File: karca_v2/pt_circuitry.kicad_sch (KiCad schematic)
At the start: 11 parts, among them U7 TLV9304xD, U8 TLV9304xD

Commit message: discrete traces
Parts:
- renumbered C19 to C34, C20 to C35
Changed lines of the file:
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@@
         )
         (path "/29cf4797-56f2-4f57-ae95-7df639362e3c/c566ee8f-cb19-4e44-a9af-dd67a0aa158e/60027281-032f-4987-83fe-1472a08d0df6"
-          (reference "R90") (unit 1)
+          (reference "R94") (unit 1)
         )
       )
@@
         )
         (path "/29cf4797-56f2-4f57-ae95-7df639362e3c/c566ee8f-cb19-4e44-a9af-dd67a0aa158e/60027281-032f-4987-83fe-1472a08d0df6"
-          (reference "R92") (unit 1)
+          (reference "R96") (unit 1)
         )
       )
@@
   (symbol (lib_id "power:GND") (at 168.656 89.916 0) (unit 1)
     (in_bom yes) (on_board yes) (dnp no) (fields_autoplaced)
-    (property "Reference" "#PWR091" (at 168.656 96.266 0)
+    (property "Reference" "#PWR0106" (at 168.656 96.266 0)
       (effects (font (size 1.27 1.27)) hide)
     )
@@
       (project "karca_v2"
         (path "/29cf4797-56f2-4f57-ae95-7df639362e3c/c566ee8f-cb19-4e44-a9af-dd67a0aa158e/044bcd6a-880d-4ffc-be8b-a03d76768183"
-          (reference "#PWR091") (unit 1)
-        )
-        (path "/29cf4797-56f2-4f57-ae95-7df639362e3c/c566ee8f-cb19-4e44-a9af-dd67a0aa158e/691cd68e-b9d2-4323-a044-22fc45a3ad38"
-          (reference "#PWR094") (unit 1)
-        )
-        (path "/29cf4797-56f2-4f57-ae95-7df639362e3c/c566ee8f-cb19-4e44-a9af-dd67a0aa158e/c6078a97-3f1f-4f19-8ed7-752ec56dbc3c"
-          (reference "#PWR097") (unit 1)
-        )
-        (path "/29cf4797-56f2-4f57-ae95-7df639362e3c/c566ee8f-cb19-4e44-a9af-dd67a0aa158e/60027281-032f-4987-83fe-1472a08d0df6"
-          (reference "#PWR0145") (unit 1)
+          (reference "#PWR0106") (unit 1)
+        )
+        (path "/29cf4797-56f2-4f57-ae95-7df639362e3c/c566ee8f-cb19-4e44-a9af-dd67a0aa158e/691cd68e-b9d2-4323-a044-22fc45a3ad38"
+          (reference "#PWR0109") (unit 1)
+        )
+        (path "/29cf4797-56f2-4f57-ae95-7df639362e3c/c566ee8f-cb19-4e44-a9af-dd67a0aa158e/c6078a97-3f1f-4f19-8ed7-752ec56dbc3c"
+          (reference "#PWR0112") (unit 1)
+        )
+        (path "/29cf4797-56f2-4f57-ae95-7df639362e3c/c566ee8f-cb19-4e44-a9af-dd67a0aa158e/60027281-032f-4987-83fe-1472a08d0df6"
+          (reference "#PWR0168") (unit 1)
         )
       )
@@
   (symbol (lib_id "Device:C") (at 191.516 58.166 270) (unit 1)
     (in_bom yes) (on_board yes) (dnp no) (fields_autoplaced)
-    (property "Reference" "C19" (at 191.516 50.546 90)
+    (property "Reference" "C34" (at 191.516 50.546 90)
       (effects (font (size 1.27 1.27)))
     )
@@
       (project "karca_v2"
         (path "/29cf4797-56f2-4f57-ae95-7df639362e3c/c566ee8f-cb19-4e44-a9af-dd67a0aa158e/044bcd6a-880d-4ffc-be8b-a03d76768183"
-          (reference "C19") (unit 1)
-        )
-        (path "/29cf4797-56f2-4f57-ae95-7df639362e3c/c566ee8f-cb19-4e44-a9af-dd67a0aa158e/691cd68e-b9d2-4323-a044-22fc45a3ad38"
-          (reference "C21") (unit 1)
-        )
-        (path "/29cf4797-56f2-4f57-ae95-7df639362e3c/c566ee8f-cb19-4e44-a9af-dd67a0aa158e/c6078a97-3f1f-4f19-8ed7-752ec56dbc3c"
-          (reference "C23") (unit 1)
-        )
-        (path "/29cf4797-56f2-4f57-ae95-7df639362e3c/c566ee8f-cb19-4e44-a9af-dd67a0aa158e/60027281-032f-4987-83fe-1472a08d0df6"
-          (reference "C49") (unit 1)
+          (reference "C34") (unit 1)
+        )
+        (path "/29cf4797-56f2-4f57-ae95-7df639362e3c/c566ee8f-cb19-4e44-a9af-dd67a0aa158e/691cd68e-b9d2-4323-a044-22fc45a3ad38"
+          (reference "C36") (unit 1)
+        )
+        (path "/29cf4797-56f2-4f57-ae95-7df639362e3c/c566ee8f-cb19-4e44-a9af-dd67a0aa158e/c6078a97-3f1f-4f19-8ed7-752ec56dbc3c"
+          (reference "C38") (unit 1)
+        )
+        (path "/29cf4797-56f2-4f57-ae95-7df639362e3c/c566ee8f-cb19-4e44-a9af-dd67a0aa158e/60027281-032f-4987-83fe-1472a08d0df6"
+          (reference "C64") (unit 1)
         )
       )
@@
   (symbol (lib_id "power:GND") (at 86.106 83.566 0) (unit 1)
     (in_bom yes) (on_board yes) (dnp no) (fields_autoplaced)
-    (property "Reference" "#PWR090" (at 86.106 89.916 0)
+    (property "Reference" "#PWR0105" (at 86.106 89.916 0)
       (effects (font (size 1.27 1.27)) hide)
     )
@@
       (project "karca_v2"
         (path "/29cf4797-56f2-4f57-ae95-7df639362e3c/c566ee8f-cb19-4e44-a9af-dd67a0aa158e/044bcd6a-880d-4ffc-be8b-a03d76768183"
-          (reference "#PWR090") (unit 1)
-        )
-        (path "/29cf4797-56f2-4f57-ae95-7df639362e3c/c566ee8f-cb19-4e44-a9af-dd67a0aa158e/691cd68e-b9d2-4323-a044-22fc45a3ad38"
-          (reference "#PWR093") (unit 1)
-        )
-        (path "/29cf4797-56f2-4f57-ae95-7df639362e3c/c566ee8f-cb19-4e44-a9af-dd67a0aa158e/c6078a97-3f1f-4f19-8ed7-752ec56dbc3c"
-          (reference "#PWR096") (unit 1)
-        )
-        (path "/29cf4797-56f2-4f57-ae95-7df639362e3c/c566ee8f-cb19-4e44-a9af-dd67a0aa158e/60027281-032f-4987-83fe-1472a08d0df6"
-          (reference "#PWR0144") (unit 1)
+          (reference "#PWR0105") (unit 1)
+        )
+        (path "/29cf4797-56f2-4f57-ae95-7df639362e3c/c566ee8f-cb19-4e44-a9af-dd67a0aa158e/691cd68e-b9d2-4323-a044-22fc45a3ad38"
+          (reference "#PWR0108") (unit 1)
+        )
+        (path "/29cf4797-56f2-4f57-ae95-7df639362e3c/c566ee8f-cb19-4e44-a9af-dd67a0aa158e/c6078a97-3f1f-4f19-8ed7-752ec56dbc3c"
+          (reference "#PWR0111") (unit 1)
+        )
+        (path "/29cf4797-56f2-4f57-ae95-7df639362e3c/c566ee8f-cb19-4e44-a9af-dd67a0aa158e/60027281-032f-4987-83fe-1472a08d0df6"
+          (reference "#PWR0167") (unit 1)
         )
       )
@@
   (symbol (lib_id "power:GND") (at 205.486 108.966 0) (unit 1)
     (in_bom yes) (on_board yes) (dnp no) (fields_autoplaced)
-    (property "Reference" "#PWR092" (at 205.486 115.316 0)
+    (property "Reference" "#PWR0107" (at 205.486 115.316 0)
       (effects (font (size 1.27 1.27)) hide)
     )
@@
       (project "karca_v2"
         (path "/29cf4797-56f2-4f57-ae95-7df639362e3c/c566ee8f-cb19-4e44-a9af-dd67a0aa158e/044bcd6a-880d-4ffc-be8b-a03d76768183"
-          (reference "#PWR092") (unit 1)
-        )
-        (path "/29cf4797-56f2-4f57-ae95-7df639362e3c/c566ee8f-cb19-4e44-a9af-dd67a0aa158e/691cd68e-b9d2-4323-a044-22fc45a3ad38"
-          (reference "#PWR095") (unit 1)
-        )
-        (path "/29cf4797-56f2-4f57-ae95-7df639362e3c/c566ee8f-cb19-4e44-a9af-dd67a0aa158e/c6078a97-3f1f-4f19-8ed7-752ec56dbc3c"
-          (reference "#PWR098") (unit 1)
-        )
-        (path "/29cf4797-56f2-4f57-ae95-7df639362e3c/c566ee8f-cb19-4e44-a9af-dd67a0aa158e/60027281-032f-4987-83fe-1472a08d0df6"
-          (reference "#PWR0146") (unit 1)
+          (reference "#PWR0107") (unit 1)
+        )
+        (path "/29cf4797-56f2-4f57-ae95-7df639362e3c/c566ee8f-cb19-4e44-a9af-dd67a0aa158e/691cd68e-b9d2-4323-a044-22fc45a3ad38"
+          (reference "#PWR0110") (unit 1)
+        )
+        (path "/29cf4797-56f2-4f57-ae95-7df639362e3c/c566ee8f-cb19-4e44-a9af-dd67a0aa158e/c6078a97-3f1f-4f19-8ed7-752ec56dbc3c"
+          (reference "#PWR0113") (unit 1)
+        )
+        (path "/29cf4797-56f2-4f57-ae95-7df639362e3c/c566ee8f-cb19-4e44-a9af-dd67a0aa158e/60027281-032f-4987-83fe-1472a08d0df6"
+          (reference "#PWR0169") (unit 1)
         )
       )
@@
         )
         (path "/29cf4797-56f2-4f57-ae95-7df639362e3c/c566ee8f-cb19-4e44-a9af-dd67a0aa158e/60027281-032f-4987-83fe-1472a08d0df6"
-          (reference "R91") (unit 1)
+          (reference "R95") (unit 1)
         )
       )
@@
         )
         (path "/29cf4797-56f2-4f57-ae95-7df639362e3c/c566ee8f-cb19-4e44-a9af-dd67a0aa158e/60027281-032f-4987-83fe-1472a08d0df6"
-          (reference "R89") (unit 1)
+          (reference "R93") (unit 1)
         )
       )
@@
   (symbol (lib_id "Device:C") (at 168.656 79.756 0) (unit 1)
     (in_bom yes) (on_board yes) (dnp no) (fields_autoplaced)
-    (property "Reference" "C20" (at 171.831 78.486 0)
+    (property "Reference" "C35" (at 171.831 78.486 0)
       (effects (font (size 1.27 1.27)) (justify left))
     )
@@
       (project "karca_v2"
         (path "/29cf4797-56f2-4f57-ae95-7df639362e3c/c566ee8f-cb19-4e44-a9af-dd67a0aa158e/044bcd6a-880d-4ffc-be8b-a03d76768183"
-          (reference "C20") (unit 1)
-        )
-        (path "/29cf4797-56f2-4f57-ae95-7df639362e3c/c566ee8f-cb19-4e44-a9af-dd67a0aa158e/691cd68e-b9d2-4323-a044-22fc45a3ad38"
-          (reference "C22") (unit 1)
-        )
-        (path "/29cf4797-56f2-4f57-ae95-7df639362e3c/c566ee8f-cb19-4e44-a9af-dd67a0aa158e/c6078a97-3f1f-4f19-8ed7-752ec56dbc3c"
-          (reference "C24") (unit 1)
-        )
-        (path "/29cf4797-56f2-4f57-ae95-7df639362e3c/c566ee8f-cb19-4e44-a9af-dd67a0aa158e/60027281-032f-4987-83fe-1472a08d0df6"
-          (reference "C50") (unit 1)
+          (reference "C35") (unit 1)
+        )
+        (path "/29cf4797-56f2-4f57-ae95-7df639362e3c/c566ee8f-cb19-4e44-a9af-dd67a0aa158e/691cd68e-b9d2-4323-a044-22fc45a3ad38"
+          (reference "C37") (unit 1)
+        )
+        (path "/29cf4797-56f2-4f57-ae95-7df639362e3c/c566ee8f-cb19-4e44-a9af-dd67a0aa158e/c6078a97-3f1f-4f19-8ed7-752ec56dbc3c"
+          (reference "C39") (unit 1)
+        )
+        (path "/29cf4797-56f2-4f57-ae95-7df639362e3c/c566ee8f-cb19-4e44-a9af-dd67a0aa158e/60027281-032f-4987-83fe-1472a08d0df6"
+          (reference "C65") (unit 1)
         )
       )
@@
         )
         (path "/29cf4797-56f2-4f57-ae95-7df639362e3c/c566ee8f-cb19-4e44-a9af-dd67a0aa158e/60027281-032f-4987-83fe-1472a08d0df6"
-          (reference "R93") (unit 1)
-        )
-      )
+          (reference "R97") (unit 1)
+        )
+      )

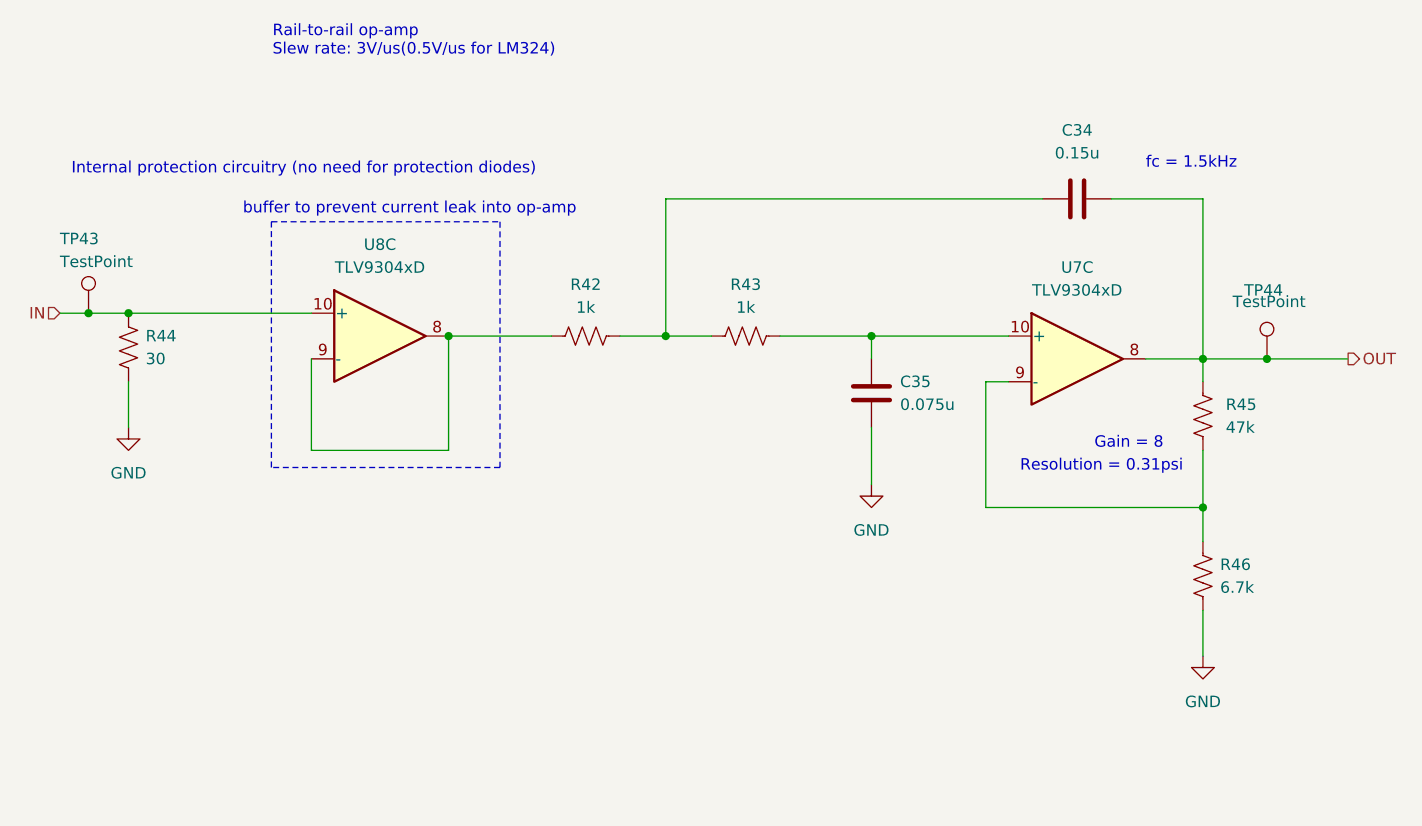
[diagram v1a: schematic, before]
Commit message: fixed TVS Diodes
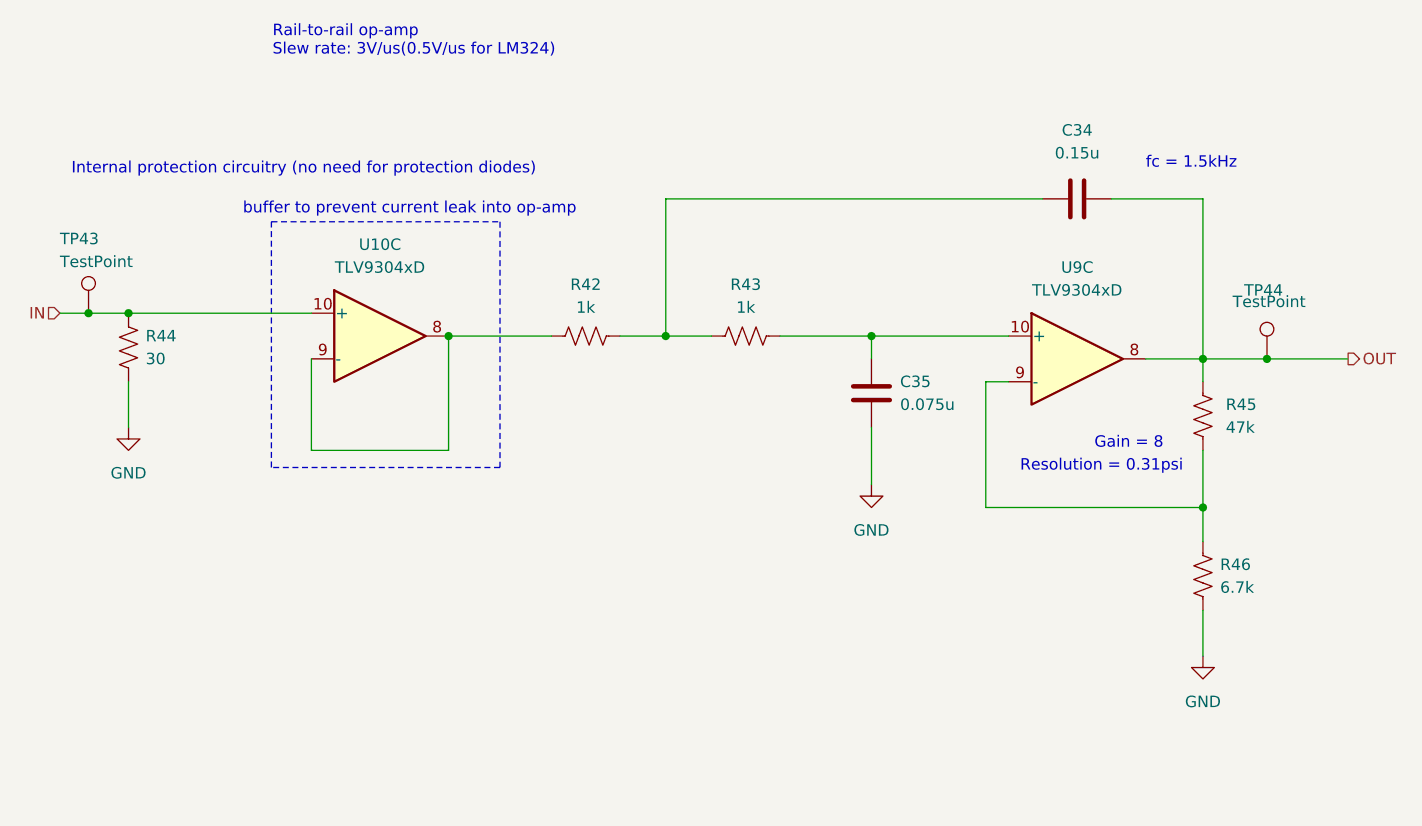
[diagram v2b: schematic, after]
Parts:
- renumbered U8 to U10, U7 to U9
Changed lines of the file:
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@@
         )
         (path "/29cf4797-56f2-4f57-ae95-7df639362e3c/c566ee8f-cb19-4e44-a9af-dd67a0aa158e/60027281-032f-4987-83fe-1472a08d0df6"
-          (reference "#PWR0168") (unit 1)
+          (reference "#PWR0160") (unit 1)
         )
       )
@@
   (symbol (lib_id "Amplifier_Operational:TLV9304xD") (at 114.046 73.406 0) (unit 3)
     (in_bom yes) (on_board yes) (dnp no) (fields_autoplaced)
-    (property "Reference" "U8" (at 114.046 63.246 0)
+    (property "Reference" "U10" (at 114.046 63.246 0)
       (effects (font (size 1.27 1.27)))
     )
@@
       (project "karca_v2"
         (path "/29cf4797-56f2-4f57-ae95-7df639362e3c/c566ee8f-cb19-4e44-a9af-dd67a0aa158e/044bcd6a-880d-4ffc-be8b-a03d76768183"
-          (reference "U8") (unit 3)
-        )
-        (path "/29cf4797-56f2-4f57-ae95-7df639362e3c/c566ee8f-cb19-4e44-a9af-dd67a0aa158e/691cd68e-b9d2-4323-a044-22fc45a3ad38"
-          (reference "U8") (unit 2)
-        )
-        (path "/29cf4797-56f2-4f57-ae95-7df639362e3c/c566ee8f-cb19-4e44-a9af-dd67a0aa158e/c6078a97-3f1f-4f19-8ed7-752ec56dbc3c"
-          (reference "U8") (unit 1)
-        )
-        (path "/29cf4797-56f2-4f57-ae95-7df639362e3c/c566ee8f-cb19-4e44-a9af-dd67a0aa158e/60027281-032f-4987-83fe-1472a08d0df6"
-          (reference "U8") (unit 4)
+          (reference "U10") (unit 3)
+        )
+        (path "/29cf4797-56f2-4f57-ae95-7df639362e3c/c566ee8f-cb19-4e44-a9af-dd67a0aa158e/691cd68e-b9d2-4323-a044-22fc45a3ad38"
+          (reference "U10") (unit 2)
+        )
+        (path "/29cf4797-56f2-4f57-ae95-7df639362e3c/c566ee8f-cb19-4e44-a9af-dd67a0aa158e/c6078a97-3f1f-4f19-8ed7-752ec56dbc3c"
+          (reference "U10") (unit 1)
+        )
+        (path "/29cf4797-56f2-4f57-ae95-7df639362e3c/c566ee8f-cb19-4e44-a9af-dd67a0aa158e/60027281-032f-4987-83fe-1472a08d0df6"
+          (reference "U10") (unit 4)
         )
       )
@@
         )
         (path "/29cf4797-56f2-4f57-ae95-7df639362e3c/c566ee8f-cb19-4e44-a9af-dd67a0aa158e/60027281-032f-4987-83fe-1472a08d0df6"
-          (reference "#PWR0167") (unit 1)
+          (reference "#PWR0159") (unit 1)
         )
       )
@@
         )
         (path "/29cf4797-56f2-4f57-ae95-7df639362e3c/c566ee8f-cb19-4e44-a9af-dd67a0aa158e/60027281-032f-4987-83fe-1472a08d0df6"
-          (reference "#PWR0169") (unit 1)
+          (reference "#PWR0161") (unit 1)
         )
       )
@@
   (symbol (lib_id "Amplifier_Operational:TLV9304xD") (at 191.516 75.946 0) (unit 3)
     (in_bom yes) (on_board yes) (dnp no) (fields_autoplaced)
-    (property "Reference" "U7" (at 191.516 65.786 0)
+    (property "Reference" "U9" (at 191.516 65.786 0)
       (effects (font (size 1.27 1.27)))
     )
@@
       (project "karca_v2"
         (path "/29cf4797-56f2-4f57-ae95-7df639362e3c/c566ee8f-cb19-4e44-a9af-dd67a0aa158e/044bcd6a-880d-4ffc-be8b-a03d76768183"
-          (reference "U7") (unit 3)
-        )
-        (path "/29cf4797-56f2-4f57-ae95-7df639362e3c/c566ee8f-cb19-4e44-a9af-dd67a0aa158e/691cd68e-b9d2-4323-a044-22fc45a3ad38"
-          (reference "U7") (unit 2)
-        )
-        (path "/29cf4797-56f2-4f57-ae95-7df639362e3c/c566ee8f-cb19-4e44-a9af-dd67a0aa158e/c6078a97-3f1f-4f19-8ed7-752ec56dbc3c"
-          (reference "U7") (unit 1)
-        )
-        (path "/29cf4797-56f2-4f57-ae95-7df639362e3c/c566ee8f-cb19-4e44-a9af-dd67a0aa158e/60027281-032f-4987-83fe-1472a08d0df6"
-          (reference "U7") (unit 4)
-        )
-      )
+          (reference "U9") (unit 3)
+        )
+        (path "/29cf4797-56f2-4f57-ae95-7df639362e3c/c566ee8f-cb19-4e44-a9af-dd67a0aa158e/691cd68e-b9d2-4323-a044-22fc45a3ad38"
+          (reference "U9") (unit 2)
+        )
+        (path "/29cf4797-56f2-4f57-ae95-7df639362e3c/c566ee8f-cb19-4e44-a9af-dd67a0aa158e/c6078a97-3f1f-4f19-8ed7-752ec56dbc3c"
+          (reference "U9") (unit 1)
+        )
+        (path "/29cf4797-56f2-4f57-ae95-7df639362e3c/c566ee8f-cb19-4e44-a9af-dd67a0aa158e/60027281-032f-4987-83fe-1472a08d0df6"
+          (reference "U9") (unit 4)
+        )
+      )

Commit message: Fixed ground capacitors
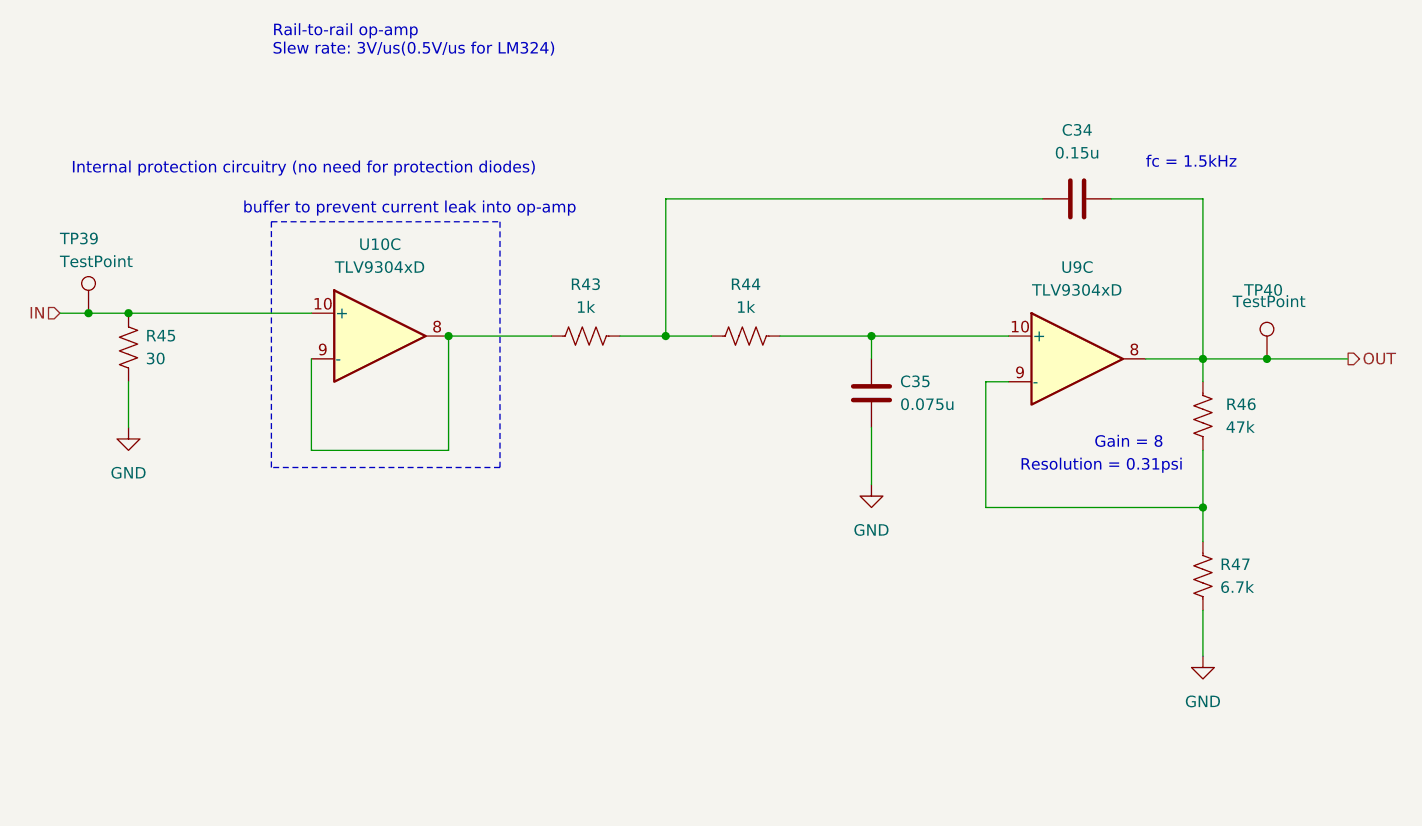
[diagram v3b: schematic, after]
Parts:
- renumbered R42 to R43, R43 to R44, R44 to R45, R45 to R46, R46 to R47, TP43 to TP39, TP44 to TP40
